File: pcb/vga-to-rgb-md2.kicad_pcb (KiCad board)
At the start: 2 copper layers, 35 x 44 mm, 11 parts, among them J1 DE15_Plug_HighDensity, J2 AudioJack3, J3 MD-90SM, U1 SN74HCS7266PWR

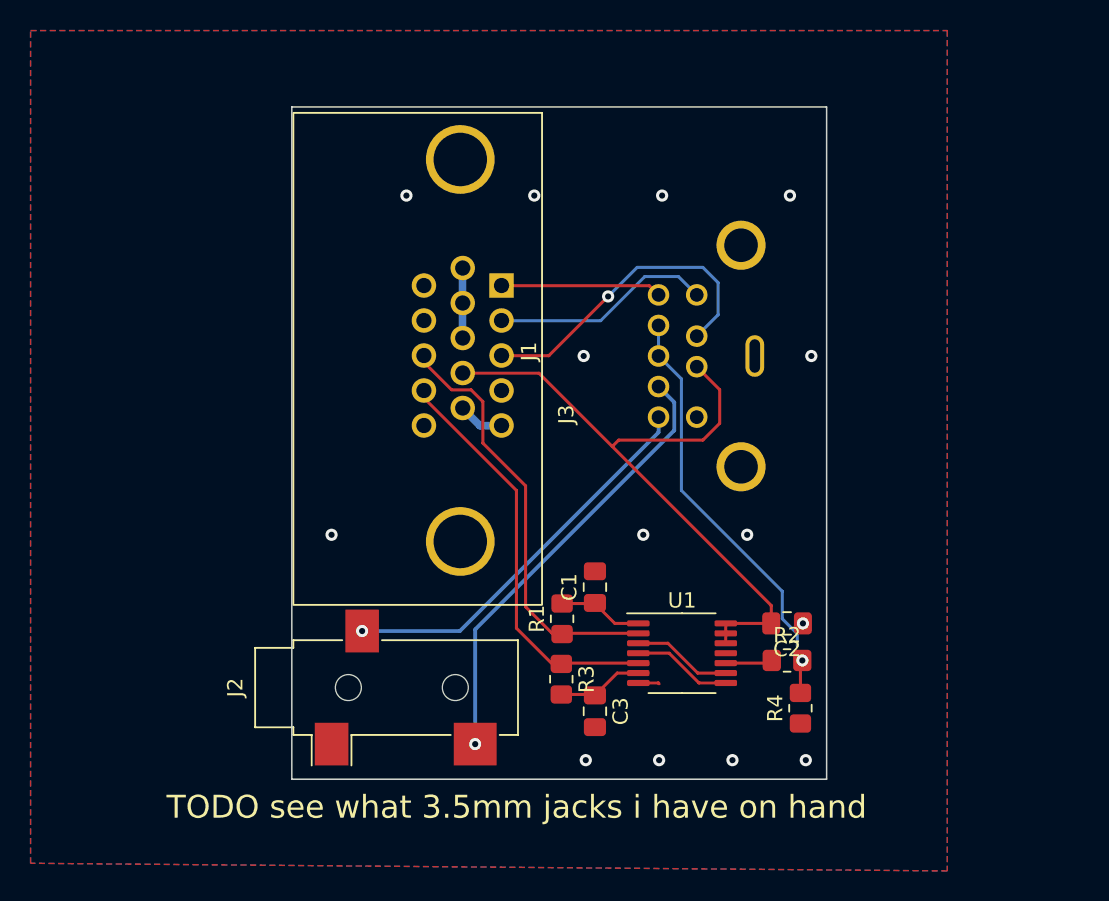
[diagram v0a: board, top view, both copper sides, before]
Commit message: Adds external 5V
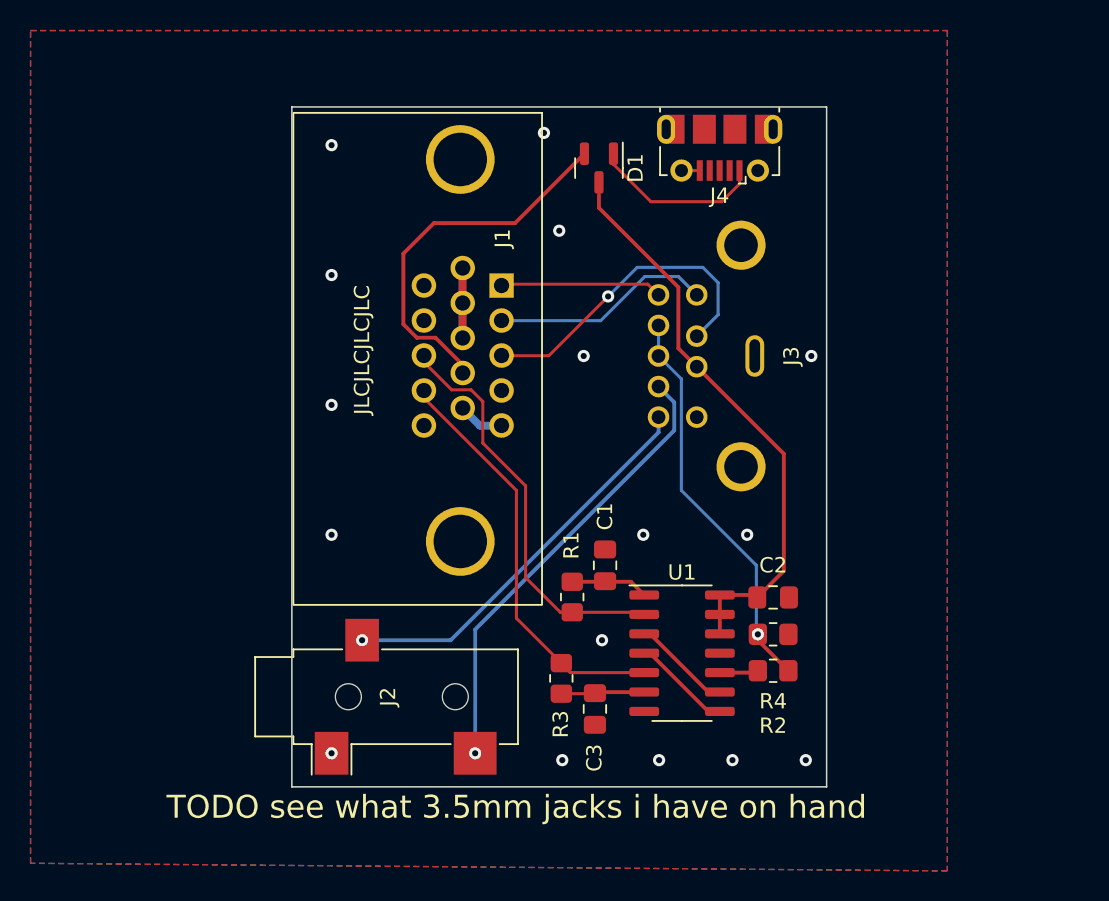
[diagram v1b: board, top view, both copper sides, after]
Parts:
- added D1: BAT54C, Package_TO_SOT_SMD:SOT-23, F.Cu at (82.2, 44.0)
- added J4: USB_B_Micro, Connector_USB:USB_Micro-B_Molex-105017-0001, F.Cu at (90.1, 42.7)
- U1: value SN74HCS7266PWR -> SN74HCS7266QDRQ1; footprint Package_SO:TSSOP-14_4.4x5mm_P0.65mm -> Package_SO:SOIC-14_3.9x8.7mm_P1.27mm
- moved R4 5.15 mm to (93.6, 74.5), turned to 180 degrees
- moved C2 1.93 mm to (93.6, 72.1)
- moved R1 1.57 mm to (80.5, 72.1)
- moved C1 1.57 mm to (82.6, 70.0)
- moved R2 1.14 mm to (93.6, 76.9)
- moved J2 0.60 mm to (68.3, 78.6)
- moved C3 0.15 mm to (81.9, 79.4)
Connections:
- J1 pad 9: VCC -> /+5V_VGA
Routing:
- net /+5V_VGA: track 0.00 -> 24.7 mm
- net Net-(J4-VBUS): track 0.00 -> 11.3 mm
- net VCC: track 43.9 -> 38.0 mm
- net GND: track 8.98 -> 13.4 mm, vias 14 -> 16
- net /IN_HSYNC: track 28.0 -> 26.8 mm
- net /IN_LAUD: track 29.2 -> 29.8 mm
- net /CSYNC_OUT: track 26.9 -> 26.4 mm
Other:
- board size 35 x 44 mm -> 35 x 44.5 mm
- board text added: "JLCJLCJLCJLC"

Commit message: Move stereo jack to face outside so VGA can sit flush against PCs
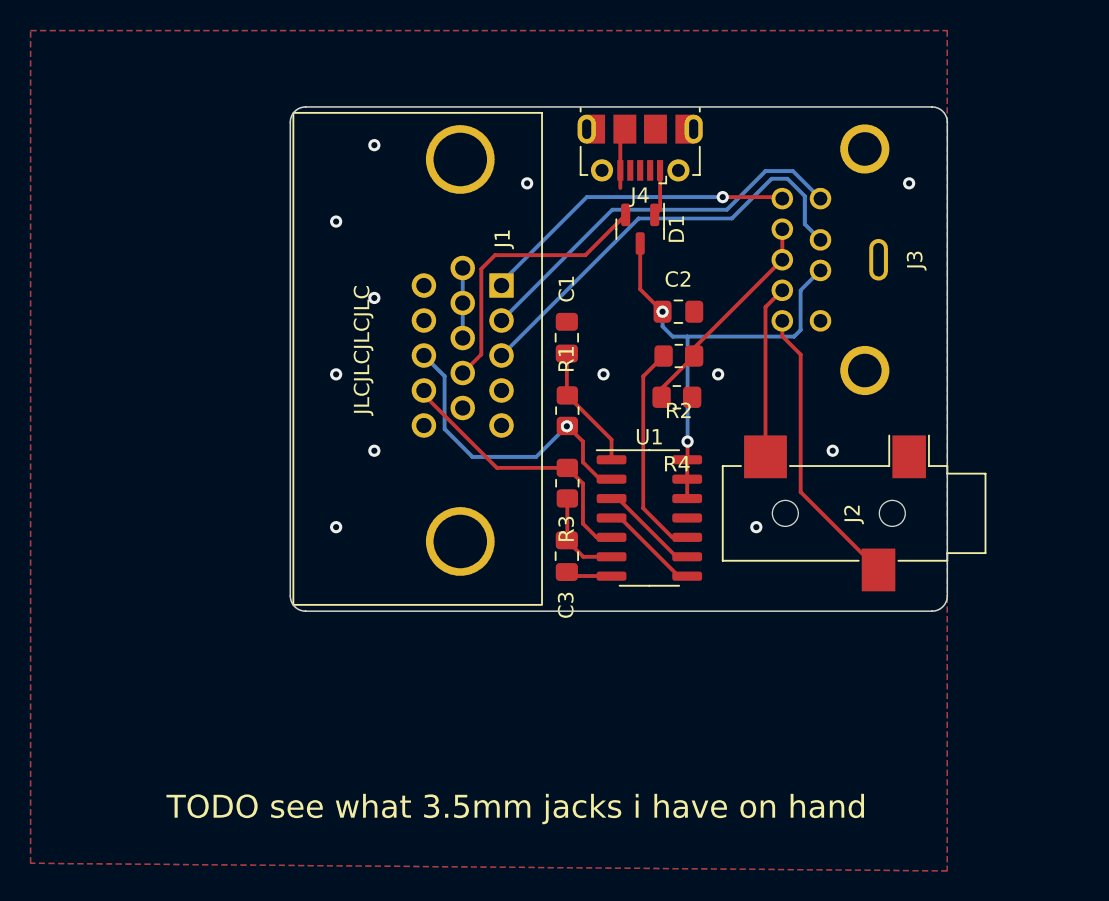
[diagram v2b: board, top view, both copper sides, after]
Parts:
- moved J2 32.9 mm to (98.9, 66.6), turned to -90 degrees
- moved R2 21.5 mm to (87.4, 56.3)
- moved C2 19.7 mm to (87.4, 53.4)
- moved R4 16.7 mm to (87.3, 59.0)
- moved C1 15.1 mm to (80.1, 55.1)
- moved R3 12.8 mm to (80.1, 64.6)
- moved R1 12.2 mm to (80.1, 59.9)
- moved J3 10.3 mm to (100.5, 50.0)
- moved C3 10.2 mm to (80.1, 69.4)
- moved U1 9.10 mm to (85.5, 66.9)
- moved J4 5.20 mm to (84.9, 42.7)
- moved D1 4.83 mm to (84.9, 48.0)
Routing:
- net /IN_LAUD: track 29.8 -> 11.4 mm, vias 1 -> 0
- net /CSYNC_OUT: track 26.4 -> 14.3 mm, vias 1 -> 0
- net Net-(U1-3Y): track 2.54 -> 14.2 mm
- net /IN_G: track 14.5 -> 25.7 mm
- net /IN_R: track 10.6 -> 20.9 mm, vias 0 -> 1
- net /IN_VSYNC: track 27.3 -> 18.0 mm
- net Net-(J4-VBUS): track 11.3 -> 3.05 mm
- net VCC: track 38.0 -> 30.6 mm, vias 0 -> 2
- net /IN_B: track 21.1 -> 28.4 mm, vias 1 -> 0
- net /IN_RAUD: track 26.0 -> 18.9 mm, vias 1 -> 0
- net /IN_HSYNC: track 26.8 -> 20.1 mm, vias 0 -> 1
- net /+5V_VGA: track 24.7 -> 18.2 mm
- net Net-(U1-1A): track 5.07 -> 8.16 mm
- net GND: track 13.4 -> 11.6 mm, vias 16 -> 12
- net Net-(U1-2B): track 5.48 -> 6.12 mm
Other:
- board size 35 x 44.5 mm -> 43 x 33 mm
